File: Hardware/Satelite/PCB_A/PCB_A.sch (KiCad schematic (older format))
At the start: 13 parts, among them J1 Batería LiPo (Soldada), J2 CONUFL001-SMD, J3 Servo Globo, J4 Conector_PCB_A-B, J5 Servo Paracaídas, Q1 SSM3J338R,LF

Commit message: PCB_A terminado
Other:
- moved on the sheet: S1
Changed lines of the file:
@@
 L power:GND #PWR08
 U 1 1 5BA1B3CD
-P 7350 3150
-F 0 "#PWR08" H 7350 2900 50  0001 C CNN
-F 1 "GND" H 7355 2977 50  0000 C CNN
-F 2 "" H 7350 3150 50  0001 C CNN
-F 3 "" H 7350 3150 50  0001 C CNN
-	1    7350 3150
+P 7600 2250
+F 0 "#PWR08" H 7600 2000 50  0001 C CNN
+F 1 "GND" H 7605 2077 50  0000 C CNN
+F 2 "" H 7600 2250 50  0001 C CNN
+F 3 "" H 7600 2250 50  0001 C CNN
+	1    7600 2250
 	1    0    0    -1
 $EndComp
@@
 L SamacSys_Parts:500SSP1S1M6QEA S1
 U 1 1 5BC7E376
-P 7350 2850
-F 0 "S1" H 7300 3350 50  0000 L CNN
-F 1 "500SSP1S1M6QEA" H 7300 3250 50  0000 L CNN
-F 2 "SamacSys_Parts:500SSP1S1M6QEA" H 8000 2950 50  0001 L CNN
-F 3 "https://www.e-switch.com/system/asset/product_line/data_sheet/115/500.pdf" H 8000 2850 50  0001 L CNN
-F 4 "Slide Switches SPDT RA SLIDE PC MNT" H 8000 2750 50  0001 L CNN "Description"
-F 5 "6" H 8000 2650 50  0001 L CNN "Height"
-F 6 "E-Switch" H 8000 2550 50  0001 L CNN "Manufacturer_Name"
-F 7 "500SSP1S1M6QEA" H 8000 2450 50  0001 L CNN "Manufacturer_Part_Number"
-F 8 "" H 8000 2350 50  0001 L CNN "RS Part Number"
-F 9 "" H 8000 2250 50  0001 L CNN "RS Price/Stock"
-F 10 "500SSP1S1M6QEA" H 8000 2150 50  0001 L CNN "Arrow Part Number"
-F 11 "" H 8000 2050 50  0001 L CNN "Arrow Price/Stock"
-	1    7350 2850
-	1    0    0    -1
-$EndComp
-Wire Wire Line
-	7300 3100 7350 3100
-Wire Wire Line
-	7350 3150 7350 3100
-Connection ~ 7350 3100
-Wire Wire Line
-	7350 3100 7400 3100
+P 7350 2750
+F 0 "S1" H 7000 2750 50  0000 L CNN
+F 1 "500SSP1S1M6QEA" H 7000 3000 50  0000 L CNN
+F 2 "SamacSys_Parts:500SSP1S1M6QEA" H 8000 2850 50  0001 L CNN
+F 3 "https://www.e-switch.com/system/asset/product_line/data_sheet/115/500.pdf" H 8000 2750 50  0001 L CNN
+F 4 "Slide Switches SPDT RA SLIDE PC MNT" H 8000 2650 50  0001 L CNN "Description"
+F 5 "6" H 8000 2550 50  0001 L CNN "Height"
+F 6 "E-Switch" H 8000 2450 50  0001 L CNN "Manufacturer_Name"
+F 7 "500SSP1S1M6QEA" H 8000 2350 50  0001 L CNN "Manufacturer_Part_Number"
+F 8 "" H 8000 2250 50  0001 L CNN "RS Part Number"
+F 9 "" H 8000 2150 50  0001 L CNN "RS Price/Stock"
+F 10 "500SSP1S1M6QEA" H 8000 2050 50  0001 L CNN "Arrow Part Number"
+F 11 "" H 8000 1950 50  0001 L CNN "Arrow Price/Stock"
+	1    7350 2750
+	-1   0    0    1
+$EndComp
 $Comp
 L power:GND #PWR011
@@
 Connection ~ 8700 2750
 Wire Wire Line
-	7150 2350 7150 2800
-Wire Wire Line
 	8350 1000 8350 2550
-Wire Wire Line
-	8350 2550 7650 2550
-Wire Wire Line
-	7650 2550 7650 2700
 Connection ~ 8350 2550
 Wire Wire Line
-	7650 2700 7550 2700
+	7150 2350 7150 2700
+Wire Wire Line
+	7550 2800 7550 2550
+Wire Wire Line
+	7550 2550 8350 2550
+Wire Wire Line
+	7300 2500 7350 2500
+Wire Wire Line
+	7350 2500 7350 2250
+Wire Wire Line
+	7350 2250 7600 2250
+Connection ~ 7350 2500
+Wire Wire Line
+	7350 2500 7400 2500
 $EndSCHEMATC

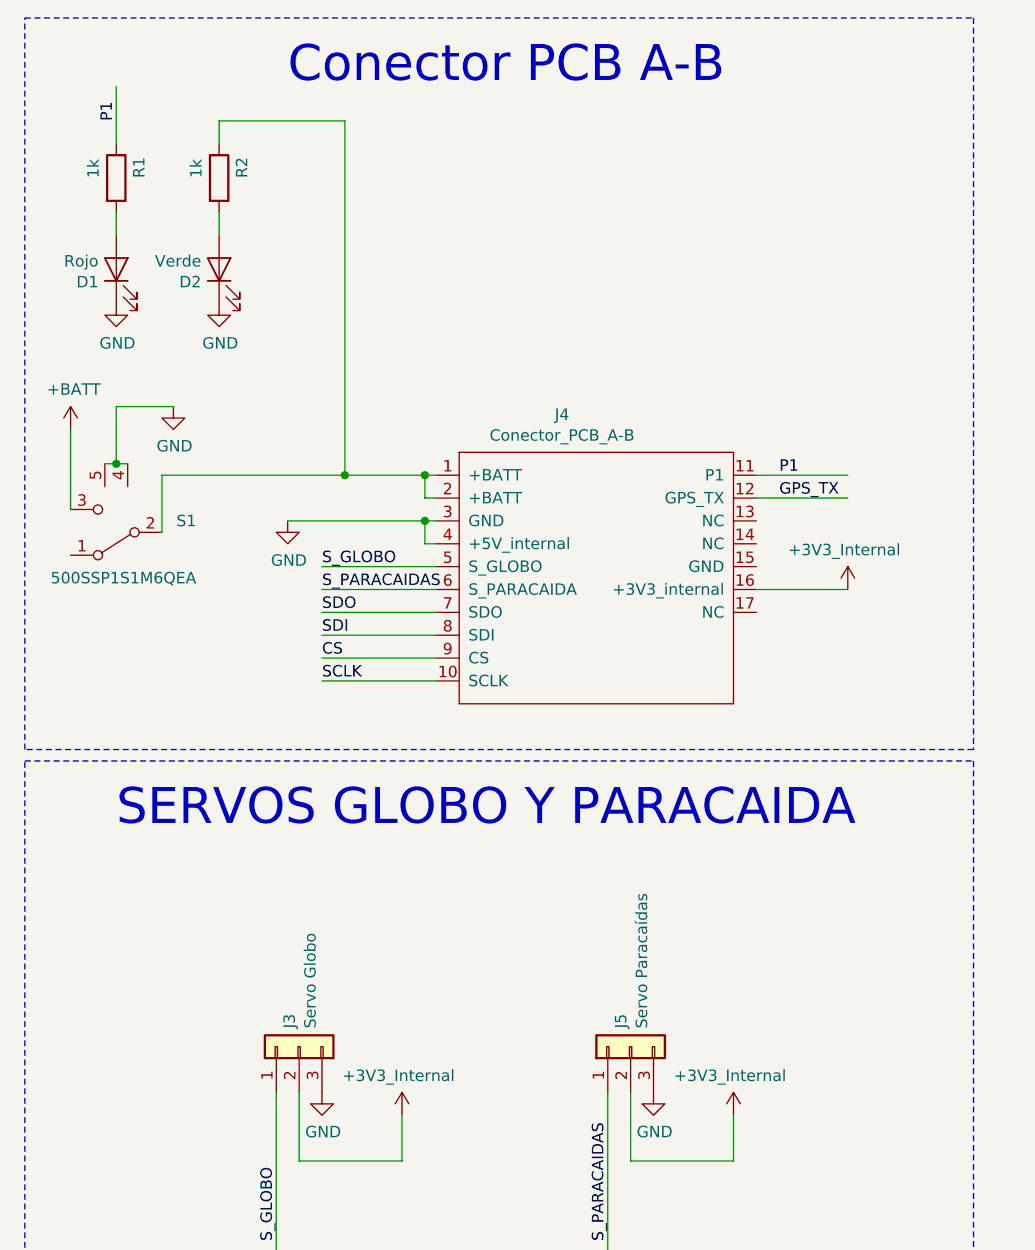
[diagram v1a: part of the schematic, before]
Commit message: Servos alimentados con 5V internos del conector A-B
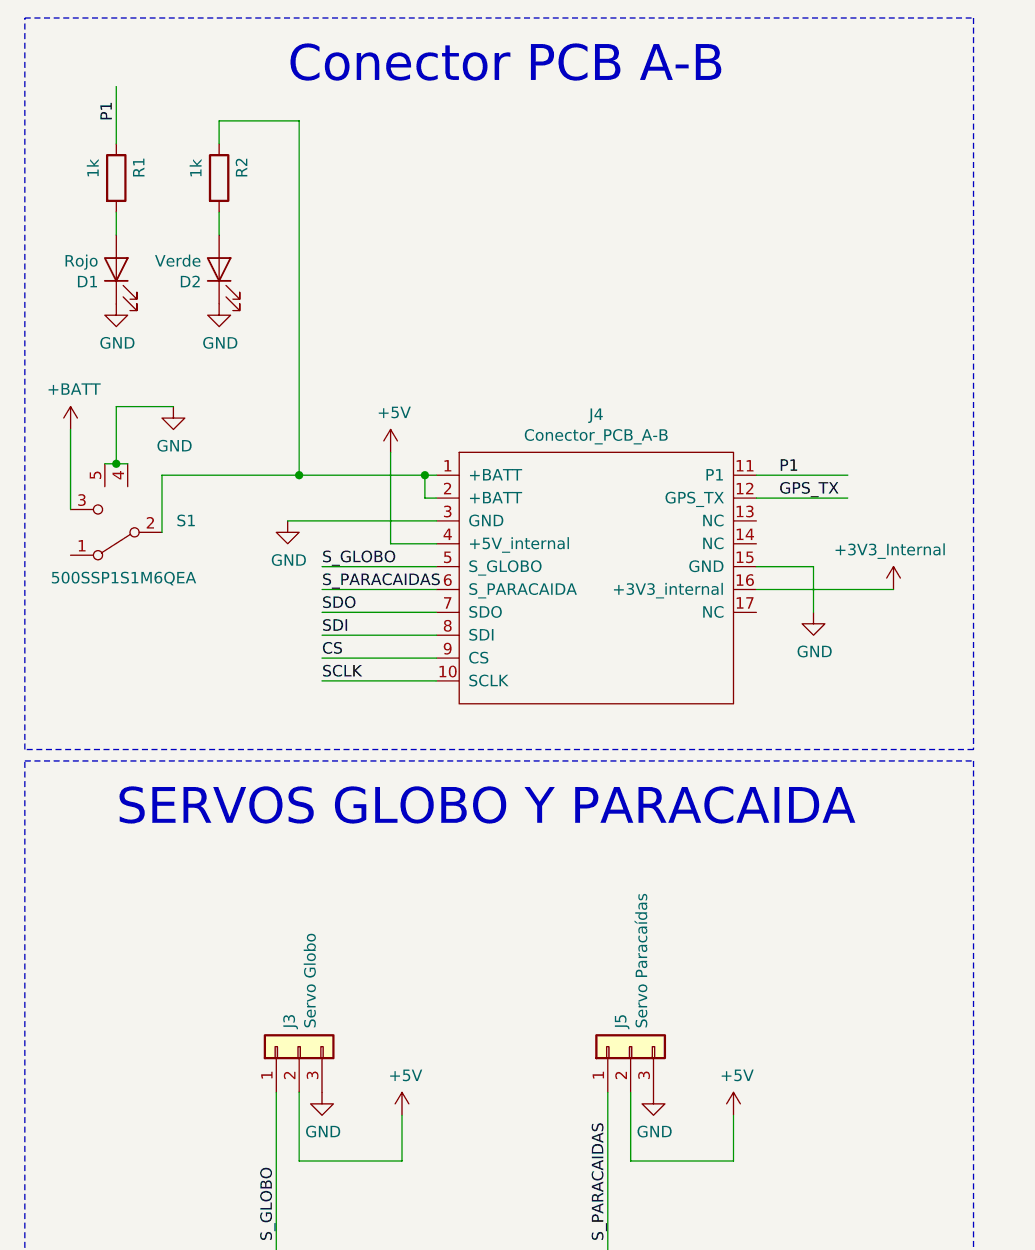
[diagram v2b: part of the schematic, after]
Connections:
- net labels added: +5V
- wire segments 61 -> 62
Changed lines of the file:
@@
 GPS_TX
 $Comp
-L power:GND #PWR08
+L power:GND #PWR09
 U 1 1 5BA1B3CD
 P 7600 2250
-F 0 "#PWR08" H 7600 2000 50  0001 C CNN
+F 0 "#PWR09" H 7600 2000 50  0001 C CNN
 F 1 "GND" H 7605 2077 50  0000 C CNN
 F 2 "" H 7600 2250 50  0001 C CNN
@@
 $EndComp
 $Comp
-L power:GND #PWR014
+L power:GND #PWR015
 U 1 1 5BAE9E59
 P 9700 5250
-F 0 "#PWR014" H 9700 5000 50  0001 C CNN
+F 0 "#PWR015" H 9700 5000 50  0001 C CNN
 F 1 "GND" H 9705 5077 50  0000 C CNN
 F 2 "" H 9700 5250 50  0001 C CNN
@@
 	7350 1500 7350 1400
 $Comp
-L power:GND #PWR09
+L power:GND #PWR08
 U 1 1 5BAFD8D0
 P 7350 1800
-F 0 "#PWR09" H 7350 1550 50  0001 C CNN
+F 0 "#PWR08" H 7350 1550 50  0001 C CNN
 F 1 "GND" H 7355 1627 50  0000 C CNN
 F 2 "" H 7350 1800 50  0001 C CNN
@@
 Wire Wire Line
 	8700 2550 8750 2550
-Wire Wire Line
-	8750 2850 8700 2850
-Wire Wire Line
-	8700 2850 8700 2750
-Wire Wire Line
-	8700 2750 8750 2750
 Text Label 8250 2950 0    50   ~ 0
 S_GLOBO
@@
 	0    -1   -1   0
 $EndComp
-$Comp
-L AXTEC_IC:+3V3_Internal #PWR13
-U 1 1 5BCA17A3
-P 8600 5350
-F 0 "#PWR13" H 8600 5750 50  0001 C CNN
-F 1 "+3V3_Internal" H 8585 5523 50  0000 C CNN
-F 2 "" H 8600 5350 50  0001 C CNN
-F 3 "" H 8600 5350 50  0001 C CNN
-	1    8600 5350
-	1    0    0    -1
-$EndComp
 Wire Wire Line
 	8600 5550 8600 5350
 Wire Wire Line
 	8150 5550 8600 5550
-$Comp
-L AXTEC_IC:+3V3_Internal #PWR15
-U 1 1 5BCA3BE2
-P 10050 5350
-F 0 "#PWR15" H 10050 5750 50  0001 C CNN
-F 1 "+3V3_Internal" H 10035 5523 50  0000 C CNN
-F 2 "" H 10050 5350 50  0001 C CNN
-F 3 "" H 10050 5350 50  0001 C CNN
-	1    10050 5350
-	1    0    0    -1
-$EndComp
 Wire Wire Line
 	10050 5550 10050 5350
@@
 	9600 5550 10050 5550
 $Comp
-L AXTEC_IC:+3V3_Internal #PWR16
+L AXTEC_IC:+3V3_Internal #PWR18
 U 1 1 5BCA5312
-P 10550 3050
-F 0 "#PWR16" H 10550 3450 50  0001 C CNN
-F 1 "+3V3_Internal" H 10535 3223 50  0000 C CNN
-F 2 "" H 10550 3050 50  0001 C CNN
-F 3 "" H 10550 3050 50  0001 C CNN
-	1    10550 3050
+P 10750 3050
+F 0 "#PWR18" H 10750 3450 50  0001 C CNN
+F 1 "+3V3_Internal" H 10735 3223 50  0000 C CNN
+F 2 "" H 10750 3050 50  0001 C CNN
+F 3 "" H 10750 3050 50  0001 C CNN
+	1    10750 3050
 	1    0    0    -1
 $EndComp
@@
 CC1101\n\n
 Wire Wire Line
-	8350 1000 7800 1000
-Wire Wire Line
 	7800 1000 7800 1100
-Wire Wire Line
-	8350 2550 8700 2550
 Text Notes 7350 4100 0    157  ~ 0
 SERVOS GLOBO Y PARACAIDA\n
@@
 Wire Wire Line
 	3300 4000 3300 4050
-$Comp
-L AXTEC_IC:Conector_PCB_A-B J4
-U 1 1 5BC66E5E
-P 9300 2850
-F 0 "J4" H 9300 3415 50  0000 C CNN
-F 1 "Conector_PCB_A-B" H 9300 3324 50  0000 C CNN
-F 2 "AXTEC:Conector_PCB_A-B" H 9050 3300 50  0001 C CNN
-F 3 "" H 9050 3300 50  0001 C CNN
-	1    9300 2850
-	1    0    0    -1
-$EndComp
 Wire Wire Line
 	8250 2950 8750 2950
@@
 Wire Wire Line
 	10150 2650 10550 2650
-Wire Wire Line
-	10150 3050 10550 3050
 $Comp
 L SamacSys_Parts:500SSP1S1M6QEA S1
@@
 $EndComp
 Wire Wire Line
-	8100 2750 8700 2750
-Connection ~ 8700 2750
-Wire Wire Line
-	8350 1000 8350 2550
-Connection ~ 8350 2550
-Wire Wire Line
 	7150 2350 7150 2700
 Wire Wire Line
 	7550 2800 7550 2550
-Wire Wire Line
-	7550 2550 8350 2550
 Wire Wire Line
 	7300 2500 7350 2500
@@
 Wire Wire Line
 	7350 2500 7400 2500
+Wire Wire Line
+	10150 3050 10750 3050
+Wire Wire Line
+	10150 2950 10400 2950
+Wire Wire Line
+	8100 2750 8750 2750
+Wire Wire Line
+	8550 2850 8550 2450
+Wire Wire Line
+	8550 2850 8750 2850
+Wire Wire Line
+	7550 2550 8150 2550
+Wire Wire Line
+	7800 1000 8150 1000
+Wire Wire Line
+	8150 1000 8150 2550
+Connection ~ 8150 2550
+Wire Wire Line
+	8150 2550 8700 2550
+$Comp
+L power:GND #PWR017
+U 1 1 5BC7DA4F
+P 10400 3150
+F 0 "#PWR017" H 10400 2900 50  0001 C CNN
+F 1 "GND" H 10405 2977 50  0000 C CNN
+F 2 "" H 10400 3150 50  0001 C CNN
+F 3 "" H 10400 3150 50  0001 C CNN
+	1    10400 3150
+	1    0    0    -1
+$EndComp
+Wire Wire Line
+	10400 3150 10400 2950
+$Comp
+L AXTEC_IC:Conector_PCB_A-B J4
+U 1 1 5BC7F6BA
+P 9300 2850
+F 0 "J4" H 9450 3415 50  0000 C CNN
+F 1 "Conector_PCB_A-B" H 9450 3324 50  0000 C CNN
+F 2 "AXTEC:Conector_PCB_A-B" H 9200 3300 50  0001 C CNN
+F 3 "" H 9200 3300 50  0001 C CNN
+	1    9300 2850
+	1    0    0    -1
+$EndComp
+$Comp
+L power:+5V #PWR0101
+U 1 1 5BC7FC2A
+P 8550 2450
+F 0 "#PWR0101" H 8550 2300 50  0001 C CNN
+F 1 "+5V" H 8565 2623 50  0000 C CNN
+F 2 "" H 8550 2450 50  0001 C CNN
+F 3 "" H 8550 2450 50  0001 C CNN
+	1    8550 2450
+	1    0    0    -1
+$EndComp
+$Comp
+L power:+5V #PWR0102
+U 1 1 5BC7FC87
+P 8600 5350
+F 0 "#PWR0102" H 8600 5200 50  0001 C CNN
+F 1 "+5V" H 8615 5523 50  0000 C CNN
+F 2 "" H 8600 5350 50  0001 C CNN
+F 3 "" H 8600 5350 50  0001 C CNN
+	1    8600 5350
+	1    0    0    -1
+$EndComp
+$Comp
+L power:+5V #PWR0103
+U 1 1 5BC7FCED
+P 10050 5350
+F 0 "#PWR0103" H 10050 5200 50  0001 C CNN
+F 1 "+5V" H 10065 5523 50  0000 C CNN
+F 2 "" H 10050 5350 50  0001 C CNN
+F 3 "" H 10050 5350 50  0001 C CNN
+	1    10050 5350
+	1    0    0    -1
+$EndComp
 $EndSCHEMATC

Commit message: Numeros de parte para PCB_A. Se movió también el switch de encendido más afuera para fácil acceso.
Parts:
- C1: Manufacturer Part Number EMK107B7104KAHT -> GRM155R61E105KA12D
- J2: Manufacturer Part Number (none) -> CONUFL001-SMD; Manufacturer_Part_Number CONUFL001-SMD -> (none)
- J3, J5: Manufacturer Part Number (none) -> 61300311121
- J4: Manufacturer Part Number 1 (none) -> 61300311121; Manufacturer Part Number 2 (none) -> 61300411121; Quantity 1 (none) -> 4; Quantity 2 (none) -> 2
- R1, R2: Manufacturer Part Number (none) -> RC0603JR-071KL
- S1: Manufacturer Part Number (none) -> 500SSP1S1M6QEA; Manufacturer_Part_Number 500SSP1S1M6QEA -> (none)
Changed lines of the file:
@@
 F 2 "Connector_PinHeader_2.54mm:PinHeader_1x03_P2.54mm_Vertical" H 9600 5050 50  0001 C CNN
 F 3 "~" H 9600 5050 50  0001 C CNN
+F 4 "61300311121" H 9600 5050 50  0001 C CNN "Manufacturer Part Number"
 	1    9600 5050
 	0    -1   -1   0
@@
 F 2 "Connector_PinHeader_2.54mm:PinHeader_1x03_P2.54mm_Vertical" H 8150 5050 50  0001 C CNN
 F 3 "~" H 8150 5050 50  0001 C CNN
+F 4 "61300311121" H 8150 5050 50  0001 C CNN "Manufacturer Part Number"
 	1    8150 5050
 	0    -1   -1   0
@@
 F 2 "Resistor_SMD:R_0603_1608Metric_Pad1.05x0.95mm_HandSolder" V 7280 1250 50  0001 C CNN
 F 3 "~" H 7350 1250 50  0001 C CNN
+F 4 "RC0603JR-071KL" V 7350 1250 50  0001 C CNN "Manufacturer Part Number"
 	1    7350 1250
 	1    0    0    -1
@@
 F 2 "Capacitor_SMD:C_0603_1608Metric_Pad1.05x0.95mm_HandSolder" H 1350 1550 50  0001 C CNN
 F 3 "~" H 1350 1550 50  0001 C CNN
-F 4 "EMK107B7104KAHT" H 1350 1550 50  0001 C CNN "Manufacturer Part Number"
+F 4 "GRM155R61E105KA12D" H 1350 1550 50  0001 C CNN "Manufacturer Part Number"
 F 5 "10V" H 1350 1550 50  0001 C CNN "Voltage"
 F 6 "X7R" H 1350 1550 50  0001 C CNN "Dielectric"
@@
 F 2 "Resistor_SMD:R_0603_1608Metric_Pad1.05x0.95mm_HandSolder" V 7730 1250 50  0001 C CNN
 F 3 "~" H 7800 1250 50  0001 C CNN
+F 4 "RC0603JR-071KL" V 7800 1250 50  0001 C CNN "Manufacturer Part Number"
 	1    7800 1250
 	1    0    0    -1
@@
 F 4 "RF Connectors / Coaxial Connectors U.FL Straight Surface Mount Jack" H 3100 3800 50  0001 L CNN "Description"
 F 5 "Linx Technologies" H 3100 3600 50  0001 L CNN "Manufacturer_Name"
-F 6 "CONUFL001-SMD" H 3100 3500 50  0001 L CNN "Manufacturer_Part_Number"
+F 6 "CONUFL001-SMD" H 3100 3500 50  0001 L CNN "Manufacturer Part Number"
 F 7 "CONUFL001-SMD" H 3100 3200 50  0001 L CNN "Arrow Part Number"
 	1    2800 3900
@@
 F 5 "6" H 8000 2550 50  0001 L CNN "Height"
 F 6 "E-Switch" H 8000 2450 50  0001 L CNN "Manufacturer_Name"
-F 7 "500SSP1S1M6QEA" H 8000 2350 50  0001 L CNN "Manufacturer_Part_Number"
-F 8 "" H 8000 2250 50  0001 L CNN "RS Part Number"
-F 9 "" H 8000 2150 50  0001 L CNN "RS Price/Stock"
-F 10 "500SSP1S1M6QEA" H 8000 2050 50  0001 L CNN "Arrow Part Number"
-F 11 "" H 8000 1950 50  0001 L CNN "Arrow Price/Stock"
+F 7 "500SSP1S1M6QEA" H 8000 2350 50  0001 L CNN "Manufacturer Part Number"
+F 8 "500SSP1S1M6QEA" H 8000 2050 50  0001 L CNN "Arrow Part Number"
 	1    7350 2750
 	-1   0    0    1
@@
 F 2 "AXTEC:Conector_PCB_A-B" H 9200 3300 50  0001 C CNN
 F 3 "" H 9200 3300 50  0001 C CNN
+F 4 "61300311121" H 9300 2850 50  0001 C CNN "Manufacturer Part Number 1"
+F 5 "4" H 9300 2850 50  0001 C CNN "Quantity 1"
+F 6 "61300411121" H 9300 2850 50  0001 C CNN "Manufacturer Part Number 2"
+F 7 "2" H 9300 2850 50  0001 C CNN "Quantity 2"
 	1    9300 2850
 	1    0    0    -1

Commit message: Agregados espaciadores a PCB_A
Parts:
- added M1, M2, M3: Spacer, AXTEC:Empty_Footprint, symbol AXTEC_IC:Spacer
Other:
- note added: "AGUJEROS DE MONTAJE"
- note removed: "AGUJEROS DE MONTAJE\n\n\n\n"
- moved on the sheet: MH1
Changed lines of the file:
@@
 L AXTEC_IC:MH_CanSat MH1
 U 1 1 5BC7973F
-P 2100 7050
-F 0 "MH1" H 2378 7165 50  0000 L CNN
-F 1 "MH_CanSat" H 2378 7074 50  0000 L CNN
-F 2 "AXTEC:MH_CanSat" H 2100 7050 50  0001 C CNN
-F 3 "" H 2100 7050 50  0001 C CNN
-	1    2100 7050
+P 1200 7200
+F 0 "MH1" H 1478 7315 50  0000 L CNN
+F 1 "MH_CanSat" H 1478 7224 50  0000 L CNN
+F 2 "AXTEC:MH_CanSat" H 1200 7200 50  0001 C CNN
+F 3 "" H 1200 7200 50  0001 C CNN
+	1    1200 7200
 	1    0    0    -1
 $EndComp
@@
 L power:GND #PWR04
 U 1 1 5BC798E1
-P 2100 7250
-F 0 "#PWR04" H 2100 7000 50  0001 C CNN
-F 1 "GND" H 2105 7077 50  0000 C CNN
-F 2 "" H 2100 7250 50  0001 C CNN
-F 3 "" H 2100 7250 50  0001 C CNN
-	1    2100 7250
-	1    0    0    -1
-$EndComp
-Wire Wire Line
-	1950 7150 1950 7200
-Wire Wire Line
-	1950 7200 2100 7200
-Wire Wire Line
-	2250 7200 2250 7150
-Wire Wire Line
-	2100 7250 2100 7200
-Connection ~ 2100 7200
-Wire Wire Line
-	2100 7200 2250 7200
-Wire Wire Line
-	2100 7150 2100 7200
+P 1200 7400
+F 0 "#PWR04" H 1200 7150 50  0001 C CNN
+F 1 "GND" H 1205 7227 50  0000 C CNN
+F 2 "" H 1200 7400 50  0001 C CNN
+F 3 "" H 1200 7400 50  0001 C CNN
+	1    1200 7400
+	1    0    0    -1
+$EndComp
+Wire Wire Line
+	1050 7300 1050 7350
+Wire Wire Line
+	1050 7350 1200 7350
+Wire Wire Line
+	1350 7350 1350 7300
+Wire Wire Line
+	1200 7400 1200 7350
+Connection ~ 1200 7350
+Wire Wire Line
+	1200 7350 1350 7350
+Wire Wire Line
+	1200 7300 1200 7350
 Wire Notes Line
 	700  6250 700  7750
@@
 Wire Notes Line
 	3600 6250 700  6250
-Text Notes 750  7250 0    157  ~ 0
-AGUJEROS DE MONTAJE\n\n\n\n
+Text Notes 800  6550 0    157  ~ 0
+AGUJEROS DE MONTAJE
 $Comp
 L SamacSys_Parts:CONUFL001-SMD J2
@@
 	1    0    0    -1
 $EndComp
+$Comp
+L AXTEC_IC:Spacer M1
+U 1 1 5C2735B7
+P 2100 7200
+F 0 "M1" H 2179 7193 50  0000 L CNN
+F 1 "Spacer" H 2179 7101 50  0000 L CNN
+F 2 "AXTEC:Empty_Footprint" H 2000 7350 50  0001 C CNN
+F 3 "https://www.mouser.com/datasheet/2/181/R30-301-1135805.pdf" H 2100 7450 50  0001 C CNN
+F 4 "R30-3010502" H 2179 7055 50  0001 L CNN "Manufacturer Part Number"
+	1    2100 7200
+	1    0    0    -1
+$EndComp
+$Comp
+L AXTEC_IC:Spacer M2
+U 1 1 5C2736D4
+P 2550 7200
+F 0 "M2" H 2629 7193 50  0000 L CNN
+F 1 "Spacer" H 2629 7101 50  0000 L CNN
+F 2 "AXTEC:Empty_Footprint" H 2450 7350 50  0001 C CNN
+F 3 "https://www.mouser.com/datasheet/2/181/R30-301-1135805.pdf" H 2550 7450 50  0001 C CNN
+F 4 "R30-3010502" H 2629 7055 50  0001 L CNN "Manufacturer Part Number"
+	1    2550 7200
+	1    0    0    -1
+$EndComp
+$Comp
+L AXTEC_IC:Spacer M3
+U 1 1 5C273720
+P 3000 7200
+F 0 "M3" H 3079 7193 50  0000 L CNN
+F 1 "Spacer" H 3079 7101 50  0000 L CNN
+F 2 "AXTEC:Empty_Footprint" H 2900 7350 50  0001 C CNN
+F 3 "https://www.mouser.com/datasheet/2/181/R30-301-1135805.pdf" H 3000 7450 50  0001 C CNN
+F 4 "R30-3010502" H 3079 7055 50  0001 L CNN "Manufacturer Part Number"
+	1    3000 7200
+	1    0    0    -1
+$EndComp

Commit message: Numeros de parte para PCB_B
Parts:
- C1: Manufacturer Part Number GRM155R61E105KA12D -> LMK107B7105MA-T
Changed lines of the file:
@@
 F 2 "Capacitor_SMD:C_0603_1608Metric_Pad1.05x0.95mm_HandSolder" H 1350 1550 50  0001 C CNN
 F 3 "~" H 1350 1550 50  0001 C CNN
-F 4 "GRM155R61E105KA12D" H 1350 1550 50  0001 C CNN "Manufacturer Part Number"
+F 4 "LMK107B7105MA-T" H 1350 1550 50  0001 C CNN "Manufacturer Part Number"
 F 5 "10V" H 1350 1550 50  0001 C CNN "Voltage"
 F 6 "X7R" H 1350 1550 50  0001 C CNN "Dielectric"

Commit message: Espaciador de 10mm para PCB_A
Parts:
- M1, M2, M3: Manufacturer Part Number R30-3010502 -> R30-3011002
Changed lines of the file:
@@
 F 2 "AXTEC:Empty_Footprint" H 2000 7350 50  0001 C CNN
 F 3 "https://www.mouser.com/datasheet/2/181/R30-301-1135805.pdf" H 2100 7450 50  0001 C CNN
-F 4 "R30-3010502" H 2179 7055 50  0001 L CNN "Manufacturer Part Number"
+F 4 "R30-3011002" H 2179 7055 50  0001 L CNN "Manufacturer Part Number"
 	1    2100 7200
 	1    0    0    -1
@@
 F 2 "AXTEC:Empty_Footprint" H 2450 7350 50  0001 C CNN
 F 3 "https://www.mouser.com/datasheet/2/181/R30-301-1135805.pdf" H 2550 7450 50  0001 C CNN
-F 4 "R30-3010502" H 2629 7055 50  0001 L CNN "Manufacturer Part Number"
+F 4 "R30-3011002" H 2629 7055 50  0001 L CNN "Manufacturer Part Number"
 	1    2550 7200
 	1    0    0    -1
@@
 F 2 "AXTEC:Empty_Footprint" H 2900 7350 50  0001 C CNN
 F 3 "https://www.mouser.com/datasheet/2/181/R30-301-1135805.pdf" H 3000 7450 50  0001 C CNN
-F 4 "R30-3010502" H 3079 7055 50  0001 L CNN "Manufacturer Part Number"
+F 4 "R30-3011002" H 3079 7055 50  0001 L CNN "Manufacturer Part Number"
 	1    3000 7200
 	1    0    0    -1

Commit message: Eliminados pines no usados del conector A-B
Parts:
- J4: Quantity 1 4 -> 3
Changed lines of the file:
@@
 F 3 "" H 9200 3300 50  0001 C CNN
 F 4 "61300311121" H 9300 2850 50  0001 C CNN "Manufacturer Part Number 1"
-F 5 "4" H 9300 2850 50  0001 C CNN "Quantity 1"
+F 5 "3" H 9300 2850 50  0001 C CNN "Quantity 1"
 F 6 "61300411121" H 9300 2850 50  0001 C CNN "Manufacturer Part Number 2"
 F 7 "2" H 9300 2850 50  0001 C CNN "Quantity 2"

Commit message: BOM para PCB_A y corrección de algunos numeros de parte
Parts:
- J4: Manufacturer Part Number (none) -> 61300311121; Manufacturer Part Number 1 61300311121 -> (none); Quantity (none) -> 3; Quantity 1 3 -> (none)
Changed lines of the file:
@@
 F 2 "AXTEC:Conector_PCB_A-B" H 9200 3300 50  0001 C CNN
 F 3 "" H 9200 3300 50  0001 C CNN
-F 4 "61300311121" H 9300 2850 50  0001 C CNN "Manufacturer Part Number 1"
-F 5 "3" H 9300 2850 50  0001 C CNN "Quantity 1"
+F 4 "61300311121" H 9300 2850 50  0001 C CNN "Manufacturer Part Number"
+F 5 "3" H 9300 2850 50  0001 C CNN "Quantity"
 F 6 "61300411121" H 9300 2850 50  0001 C CNN "Manufacturer Part Number 2"
 F 7 "2" H 9300 2850 50  0001 C CNN "Quantity 2"
